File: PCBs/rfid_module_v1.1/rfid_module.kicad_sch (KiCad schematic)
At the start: 2 parts, among them U101 Watch_Module_Outline_V2

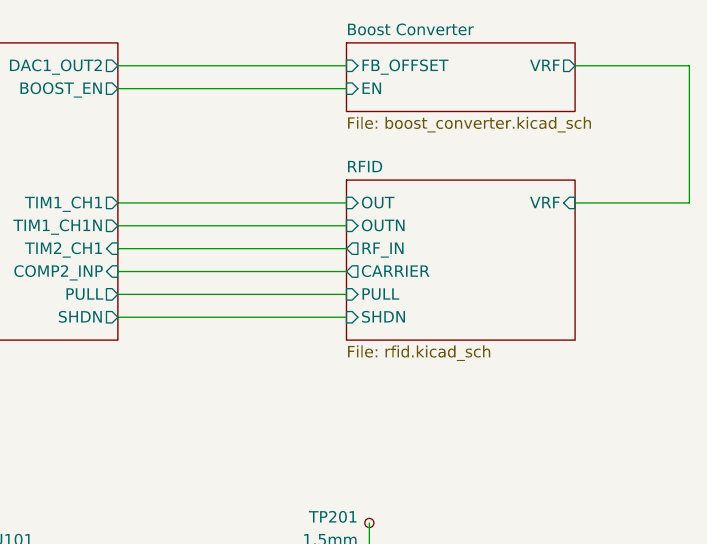
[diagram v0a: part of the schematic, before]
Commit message: RFID Module v1.1 complete (+default firmware)
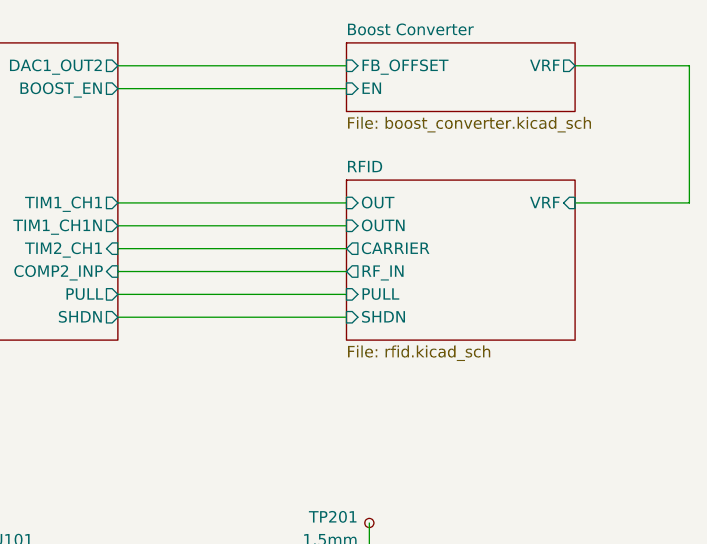
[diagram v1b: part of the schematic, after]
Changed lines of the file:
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@@
     (rev "1.1")
   )
+  (wire (pts (xy 215.9 93.98) (xy 228.6 93.98))
+    (stroke (width 0) (type default))
+  )
+  (wire (pts (xy 104.14 78.74) (xy 129.54 78.74))
+    (stroke (width 0) (type default))
+  )
+  (wire (pts (xy 165.1 78.74) (xy 190.5 78.74))
+    (stroke (width 0) (type default))
+  )
+  (wire (pts (xy 228.6 78.74) (xy 228.6 93.98))
+    (stroke (width 0) (type default))
+  )
+  (wire (pts (xy 104.14 96.52) (xy 129.54 96.52))
+    (stroke (width 0) (type default))
+  )
+  (wire (pts (xy 104.14 93.98) (xy 129.54 93.98))
+    (stroke (width 0) (type default))
+  )
   (wire (pts (xy 165.1 99.06) (xy 190.5 99.06))
     (stroke (width 0) (type default))
   )
+  (wire (pts (xy 104.14 88.9) (xy 129.54 88.9))
+    (stroke (width 0) (type default))
+  )
+  (wire (pts (xy 104.14 86.36) (xy 129.54 86.36))
+    (stroke (width 0) (type default))
+  )
+  (wire (pts (xy 193.04 129.54) (xy 193.04 132.08))
+    (stroke (width 0) (type default))
+  )
+  (wire (pts (xy 104.14 81.28) (xy 129.54 81.28))
+    (stroke (width 0) (type default))
+  )
+  (wire (pts (xy 165.1 104.14) (xy 190.5 104.14))
+    (stroke (width 0) (type default))
+  )
   (wire (pts (xy 165.1 101.6) (xy 190.5 101.6))
-    (stroke (width 0) (type default))
-  )
-  (wire (pts (xy 215.9 93.98) (xy 228.6 93.98))
-    (stroke (width 0) (type default))
-  )
-  (wire (pts (xy 104.14 78.74) (xy 129.54 78.74))
-    (stroke (width 0) (type default))
-  )
-  (wire (pts (xy 165.1 78.74) (xy 190.5 78.74))
-    (stroke (width 0) (type default))
-  )
-  (wire (pts (xy 228.6 78.74) (xy 228.6 93.98))
-    (stroke (width 0) (type default))
-  )
-  (wire (pts (xy 104.14 96.52) (xy 129.54 96.52))
-    (stroke (width 0) (type default))
-  )
-  (wire (pts (xy 104.14 93.98) (xy 129.54 93.98))
-    (stroke (width 0) (type default))
-  )
-  (wire (pts (xy 104.14 88.9) (xy 129.54 88.9))
-    (stroke (width 0) (type default))
-  )
-  (wire (pts (xy 104.14 86.36) (xy 129.54 86.36))
-    (stroke (width 0) (type default))
-  )
-  (wire (pts (xy 193.04 129.54) (xy 193.04 132.08))
-    (stroke (width 0) (type default))
-  )
-  (wire (pts (xy 104.14 81.28) (xy 129.54 81.28))
-    (stroke (width 0) (type default))
-  )
-  (wire (pts (xy 165.1 104.14) (xy 190.5 104.14))
     (stroke (width 0) (type default))
   )
@@
       (effects (font (size 1.27 1.27)) (justify left))
     )
-    (pin "RF_IN" output (at 190.5 99.06 180)
-      (effects (font (size 1.27 1.27)) (justify left))
-    )
-    (pin "CARRIER" output (at 190.5 101.6 180)
-      (effects (font (size 1.27 1.27)) (justify left))
-    )
+    (pin "RF_IN" output (at 190.5 101.6 180)
+      (effects (font (size 1.27 1.27)) (justify left))
+    )
+    (pin "CARRIER" output (at 190.5 99.06 180)
+      (effects (font (size 1.27 1.27)) (justify left))
+    )

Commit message: PCB V3 progress
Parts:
- renumbered TP201 to TP101
